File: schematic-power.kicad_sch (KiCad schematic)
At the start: 32 parts, among them U4 TPS62933, U9 TPS62933

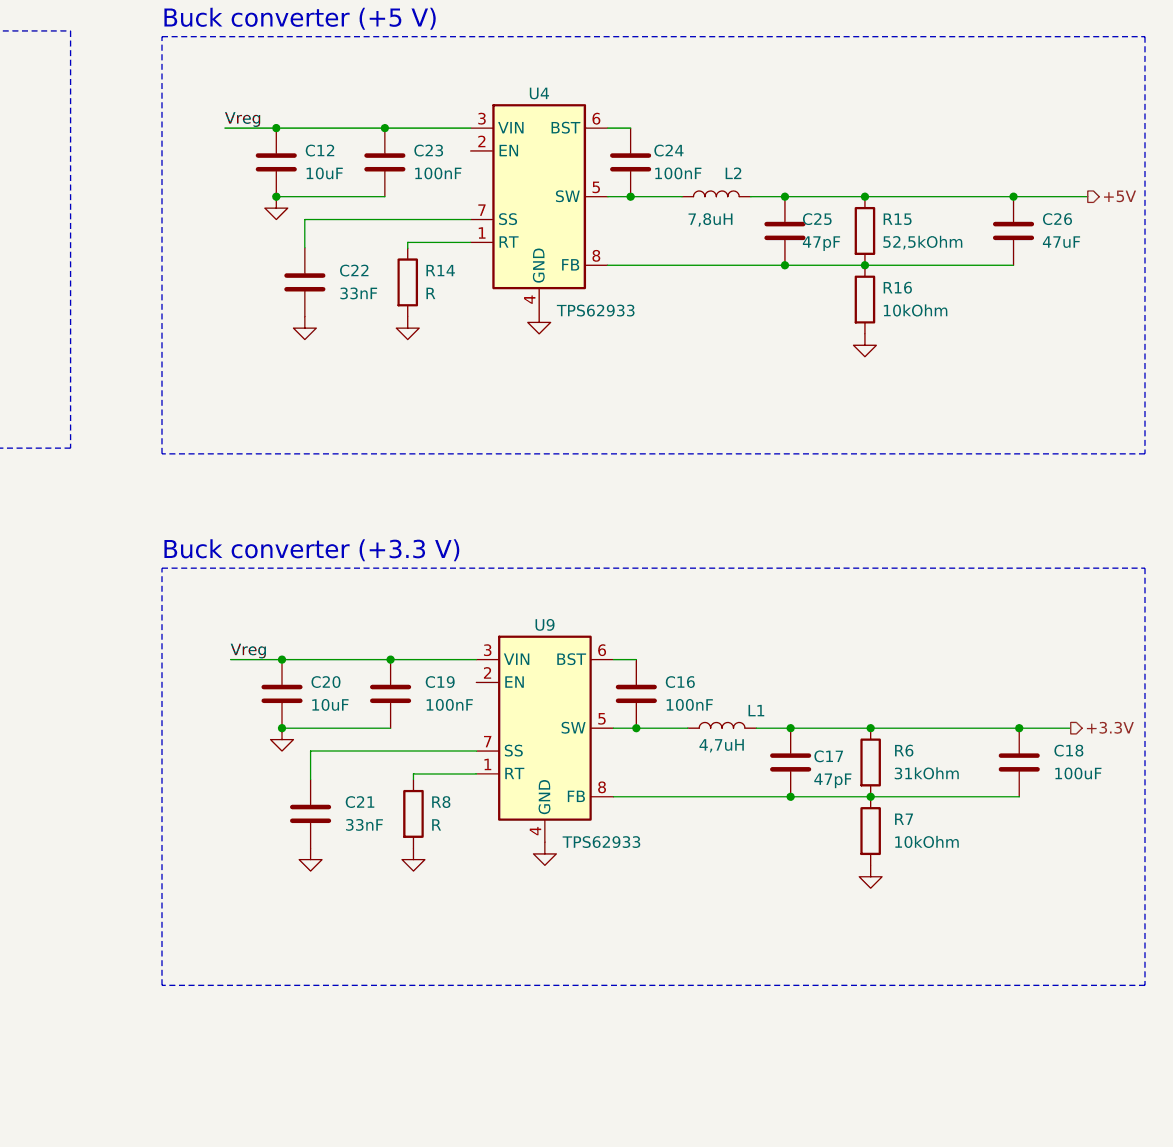
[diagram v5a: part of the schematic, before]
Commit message: Configuration of RT pins for buck converters
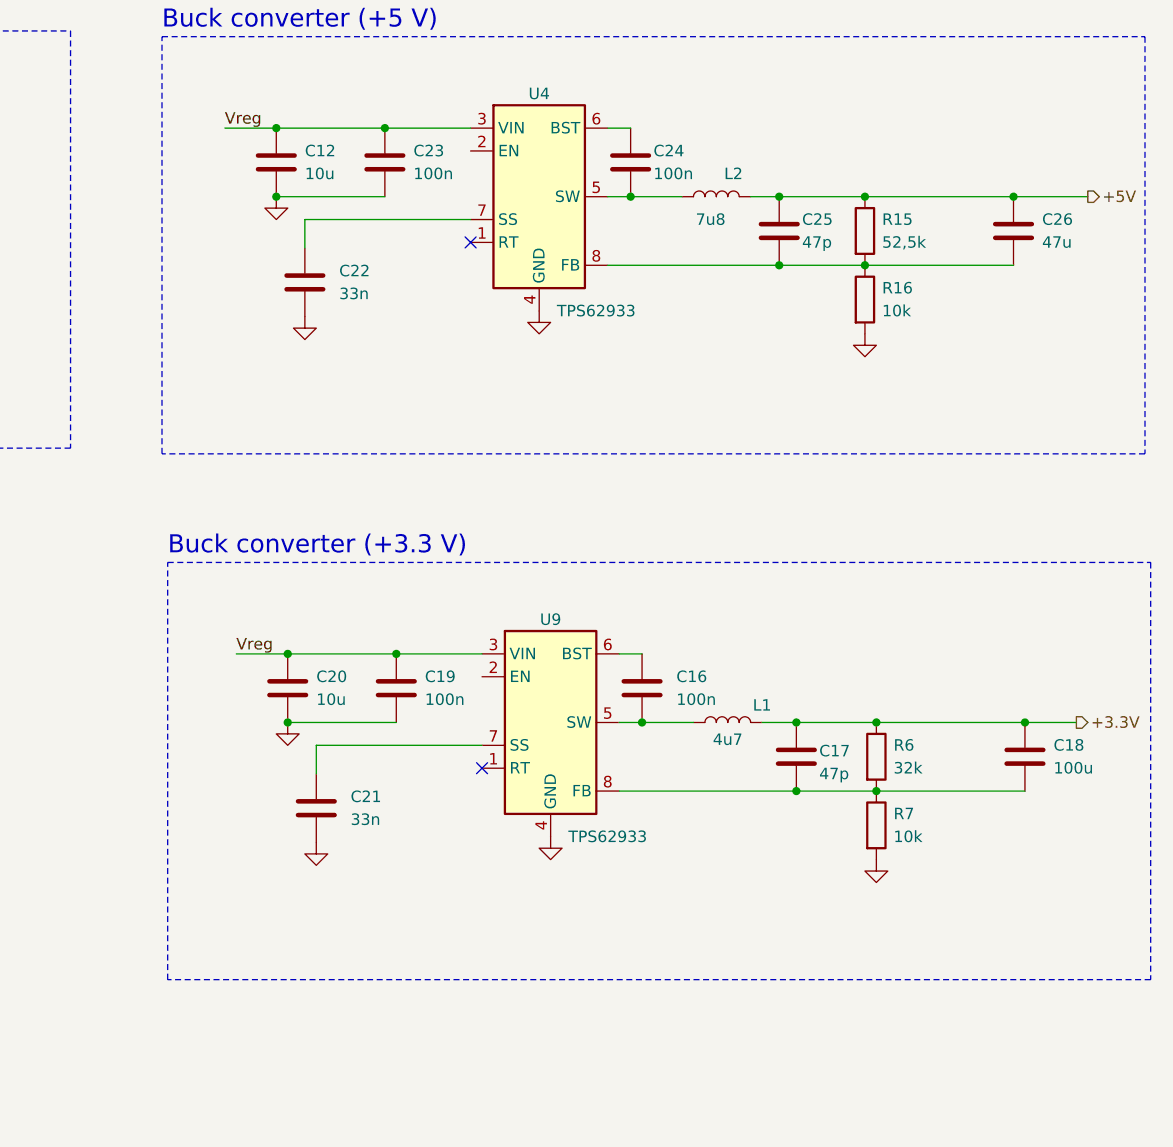
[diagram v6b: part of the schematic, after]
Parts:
- removed R14, R8: R, symbol Device:R
- C12, C20: value 10uF -> 10u
- C16, C19, C23, C24: value 100nF -> 100n
- C17, C25: value 47pF -> 47p
- C18: value 100uF -> 100u
- C21, C22: value 33nF -> 33n
- C26: value 47uF -> 47u
- L1: value 4,7uH -> 4u7
- L2: value 7,8uH -> 7u8
- R15: value 52,5kOhm -> 52,5k
- R16, R7: value 10kOhm -> 10k
- R6: value 31kOhm -> 32k
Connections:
- no-connect marks 1 -> 3
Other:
- moved on the sheet: C16, C17, C18, C19, C20, C21, C25, L1, R6, R7, U9

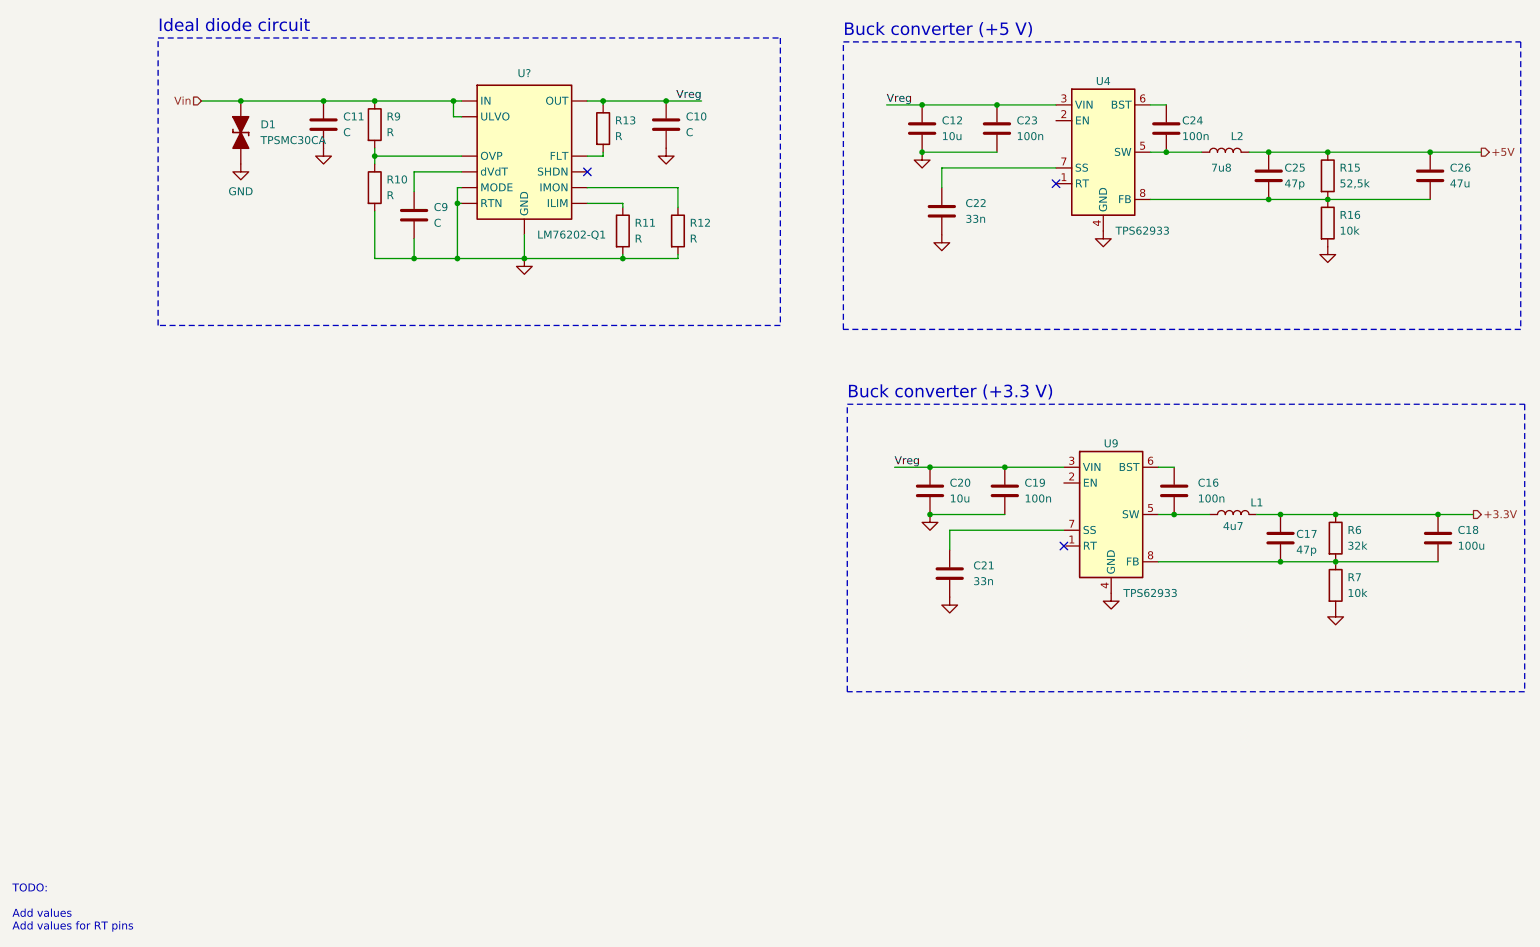
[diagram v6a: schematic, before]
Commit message: Add value for Cdvdt capacitor for ideal diode
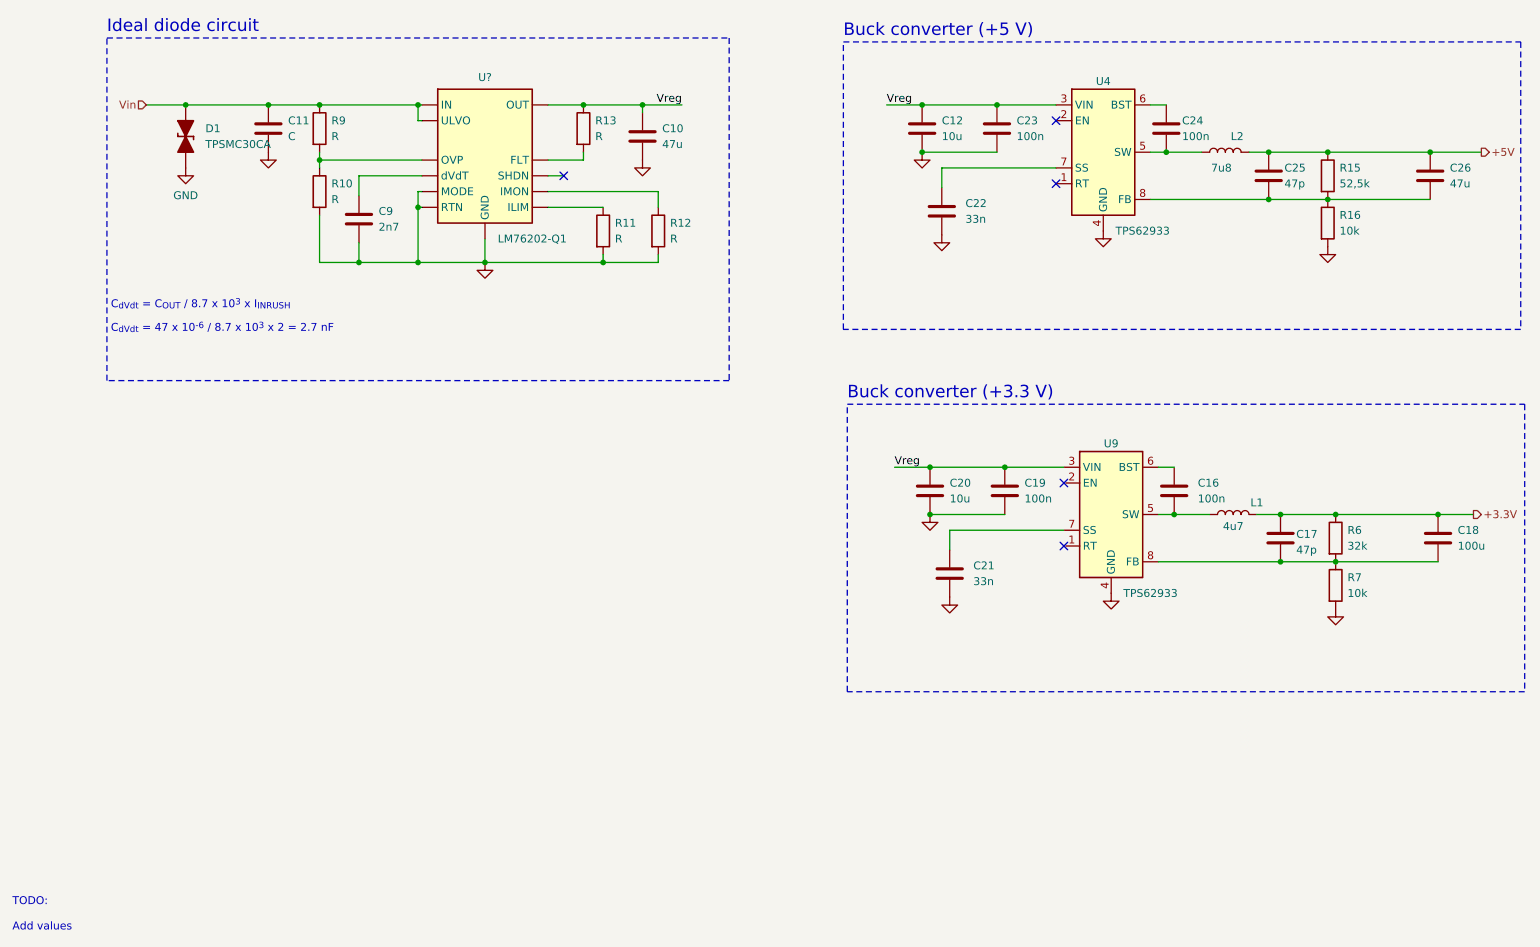
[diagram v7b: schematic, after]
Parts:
- C10: value C -> 47u
- C9: value C -> 2n7
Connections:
- no-connect marks 3 -> 5
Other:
- note added: "C_{dVdt} = 47 x 10^{-6} / 8.7 x 10^{3} x 2 = 2.7 nF"
- note added: "C_{dVdt} = C_{OUT} / 8.7 x 10^{3} x I_{INRUSH}"
- note added: "TODO: Add values"
- note removed: "TODO: Add values Add values for RT pins"
- moved on the sheet: C10, C11, C9, D1, R10, R11, R12, R13, R9, U?
